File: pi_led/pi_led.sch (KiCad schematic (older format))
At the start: 12 parts, among them CON1 PWR, P1 LED_STRIP, P2 RiPi, Q1 Q_NMOS_GDS, Q2 Q_NMOS_GDS, Q3 Q_NMOS_GDS

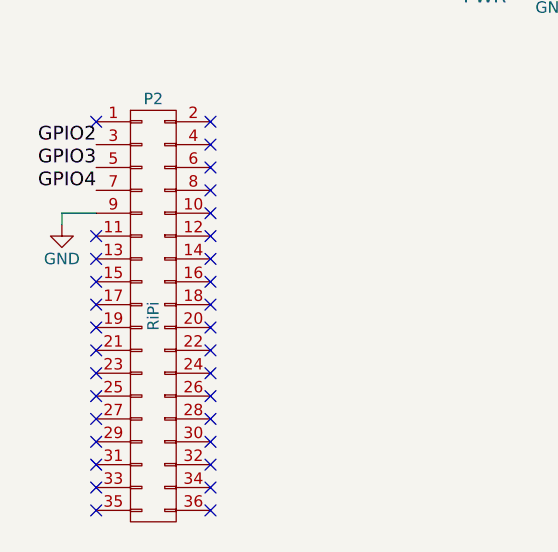
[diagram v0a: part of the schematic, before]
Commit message: Add more GND, add board info
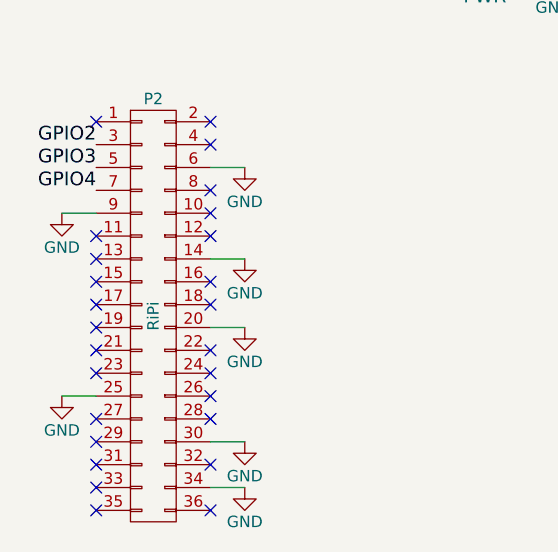
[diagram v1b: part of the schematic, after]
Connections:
- net GND: now also P2.14 (P14), P2.20 (P20), P2.25 (P25), P2.30 (P30), P2.34 (P34), P2.6 (P6)
- no-connect marks 32 -> 26
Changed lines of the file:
@@
 EESchema Schematic File Version 2
-LIBS:power
-LIBS:device
-LIBS:transistors
-LIBS:conn
-LIBS:linear
-LIBS:regul
-LIBS:74xx
-LIBS:cmos4000
-LIBS:adc-dac
-LIBS:memory
-LIBS:xilinx
-LIBS:microcontrollers
-LIBS:dsp
-LIBS:microchip
-LIBS:analog_switches
-LIBS:motorola
-LIBS:texas
-LIBS:intel
-LIBS:audio
-LIBS:interface
-LIBS:digital-audio
-LIBS:philips
-LIBS:display
-LIBS:cypress
-LIBS:siliconi
-LIBS:opto
-LIBS:atmel
-LIBS:contrib
-LIBS:valves
 LIBS:pi_led-cache
 EELAYER 25 0
@@
 L GND #PWR03
 U 1 1 55CE5B82
-P 2350 3700
-F 0 "#PWR03" H 2350 3450 50  0001 C CNN
-F 1 "GND" H 2350 3550 50  0000 C CNN
-F 2 "" H 2350 3700 60  0000 C CNN
-F 3 "" H 2350 3700 60  0000 C CNN
-	1    2350 3700
+P 2350 3650
+F 0 "#PWR03" H 2350 3400 50  0001 C CNN
+F 1 "GND" H 2350 3500 50  0000 C CNN
+F 2 "" H 2350 3650 60  0000 C CNN
+F 3 "" H 2350 3650 60  0000 C CNN
+	1    2350 3650
 	1    0    0    -1
 $EndComp
@@
 Wire Wire Line
 	4500 2600 4800 2600
-NoConn ~ 3000 3450
 NoConn ~ 3000 3550
 NoConn ~ 3000 3650
 NoConn ~ 3000 3750
-NoConn ~ 3000 3850
 NoConn ~ 3000 3950
 NoConn ~ 3000 4050
-NoConn ~ 3000 4150
 NoConn ~ 3000 4250
 NoConn ~ 3000 4350
 NoConn ~ 3000 4450
-NoConn ~ 2500 4450
 NoConn ~ 2500 4350
 NoConn ~ 2500 4250
@@
 NoConn ~ 2500 3250
 Wire Wire Line
-	2350 3700 2350 3650
-Wire Wire Line
 	2350 3650 2500 3650
 NoConn ~ 3000 3250
@@
 NoConn ~ 2500 4950
 NoConn ~ 3000 4950
-NoConn ~ 3000 4850
 NoConn ~ 3000 4750
-NoConn ~ 3000 4650
 NoConn ~ 3000 4550
+$Comp
+L GND #PWR?
+U 1 1 55CF715D
+P 3150 3450
+F 0 "#PWR?" H 3150 3200 50  0001 C CNN
+F 1 "GND" H 3150 3300 50  0000 C CNN
+F 2 "" H 3150 3450 60  0000 C CNN
+F 3 "" H 3150 3450 60  0000 C CNN
+	1    3150 3450
+	1    0    0    -1
+$EndComp
+$Comp
+L GND #PWR?
+U 1 1 55CF718C
+P 3150 3850
+F 0 "#PWR?" H 3150 3600 50  0001 C CNN
+F 1 "GND" H 3150 3700 50  0000 C CNN
+F 2 "" H 3150 3850 60  0000 C CNN
+F 3 "" H 3150 3850 60  0000 C CNN
+	1    3150 3850
+	1    0    0    -1
+$EndComp
+Wire Wire Line
+	3000 3450 3150 3450
+Wire Wire Line
+	3000 3850 3150 3850
+$Comp
+L GND #PWR?
+U 1 1 55CF7228
+P 3150 4150
+F 0 "#PWR?" H 3150 3900 50  0001 C CNN
+F 1 "GND" H 3150 4000 50  0000 C CNN
+F 2 "" H 3150 4150 60  0000 C CNN
+F 3 "" H 3150 4150 60  0000 C CNN
+	1    3150 4150
+	1    0    0    -1
+$EndComp
+$Comp
+L GND #PWR?
+U 1 1 55CF7257
+P 2350 4450
+F 0 "#PWR?" H 2350 4200 50  0001 C CNN
+F 1 "GND" H 2350 4300 50  0000 C CNN
+F 2 "" H 2350 4450 60  0000 C CNN
+F 3 "" H 2350 4450 60  0000 C CNN
+	1    2350 4450
+	1    0    0    -1
+$EndComp
+Wire Wire Line
+	3000 4150 3150 4150
+Wire Wire Line
+	2500 4450 2350 4450
+$Comp
+L GND #PWR?
+U 1 1 55CF7347
+P 3150 4650
+F 0 "#PWR?" H 3150 4400 50  0001 C CNN
+F 1 "GND" H 3150 4500 50  0000 C CNN
+F 2 "" H 3150 4650 60  0000 C CNN
+F 3 "" H 3150 4650 60  0000 C CNN
+	1    3150 4650
+	1    0    0    -1
+$EndComp
+$Comp
+L GND #PWR?
+U 1 1 55CF7376
+P 3150 4850
+F 0 "#PWR?" H 3150 4600 50  0001 C CNN
+F 1 "GND" H 3150 4700 50  0000 C CNN
+F 2 "" H 3150 4850 60  0000 C CNN
+F 3 "" H 3150 4850 60  0000 C CNN
+	1    3150 4850
+	1    0    0    -1
+$EndComp
+Wire Wire Line
+	3000 4850 3150 4850
+Wire Wire Line
+	3000 4650 3150 4650
 $EndSCHEMATC

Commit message: Added part # to MOSFETs in schematic
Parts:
- Q1, Q2, Q3: value Q_NMOS_GDS -> STP16NF06L
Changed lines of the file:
@@
 EESchema Schematic File Version 2
+LIBS:power
+LIBS:device
+LIBS:transistors
+LIBS:conn
+LIBS:linear
+LIBS:regul
+LIBS:74xx
+LIBS:cmos4000
+LIBS:adc-dac
+LIBS:memory
+LIBS:xilinx
+LIBS:microcontrollers
+LIBS:dsp
+LIBS:microchip
+LIBS:analog_switches
+LIBS:motorola
+LIBS:texas
+LIBS:intel
+LIBS:audio
+LIBS:interface
+LIBS:digital-audio
+LIBS:philips
+LIBS:display
+LIBS:cypress
+LIBS:siliconi
+LIBS:opto
+LIBS:atmel
+LIBS:contrib
+LIBS:valves
 LIBS:pi_led-cache
 EELAYER 25 0
@@
 P 7550 3000
 F 0 "Q3" H 7850 3050 50  0000 R CNN
-F 1 "Q_NMOS_GDS" H 8200 2950 50  0001 R CNN
+F 1 "STP16NF06L" H 8200 2950 50  0001 R CNN
 F 2 "Transistors_TO-220:TO-220_Neutral123_Horizontal" H 7750 3100 29  0001 C CNN
 F 3 "" H 7550 3000 60  0000 C CNN
@@
 P 6450 3000
 F 0 "Q2" H 6750 3050 50  0000 R CNN
-F 1 "Q_NMOS_GDS" H 7100 2950 50  0001 R CNN
+F 1 "STP16NF06L" H 7100 2950 50  0001 R CNN
 F 2 "Transistors_TO-220:TO-220_Neutral123_Horizontal" H 6650 3100 29  0001 C CNN
 F 3 "" H 6450 3000 60  0000 C CNN
@@
 P 5350 3000
 F 0 "Q1" H 5650 3050 50  0000 R CNN
-F 1 "Q_NMOS_GDS" H 6000 2950 50  0001 R CNN
+F 1 "STP16NF06L" H 6000 2950 50  0001 R CNN
 F 2 "Transistors_TO-220:TO-220_Neutral123_Horizontal" H 5550 3100 29  0001 C CNN
 F 3 "" H 5350 3000 60  0000 C CNN

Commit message: Replaced barrel jack part, no slots
Removed slots from barrel jack part because I don't think Dirty PCBs handles
plated slots nicely.

Tweaked LED_B track because clearance was a little close for comfort

Removed backup file.
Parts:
- CON1: footprint Connect:BARREL_JACK -> barrel_jack:barrel_jack
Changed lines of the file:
@@
 F 0 "CON1" H 4200 2750 60  0000 C CNN
 F 1 "PWR" H 4200 2300 60  0000 C CNN
-F 2 "Connect:BARREL_JACK" H 4200 2500 60  0001 C CNN
+F 2 "barrel_jack:barrel_jack" H 4200 2500 60  0001 C CNN
 F 3 "" H 4200 2500 60  0000 C CNN
 	1    4200 2500
